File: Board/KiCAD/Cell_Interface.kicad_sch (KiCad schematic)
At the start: 32 parts, among them Q23 2N7002, Q24 2N7002, Q25 2N7002, Q26 2N7002, Q27 IRF9540NSTRLPBF, Q28 IRF9540NSTRLPBF, Q29 IRF9540NSTRLPBF, Q30 IRF9540NSTRLPBF, Q31 IRF9540NSTRLPBF, Q32 2N7002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

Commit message: Add files via upload
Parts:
- removed Q31, Q33: IRF9540NSTRLPBF, IRF9540NSTRLPBF:DPAK254P1524X483-4_3N, symbol IRF9540NSTRLPBF:IRF9540NSTRLPBF
- removed Q32: 2N7002, Package_TO_SOT_SMD:SOT-23, symbol Transistor_FET:2N7002
- removed R70: R_Small, symbol Device:R_Small
- removed R71: R_Small, Resistor_SMD:R_0201_0603Metric, symbol Device:R_Small
- added C49, C50: 100n, Capacitor_SMD:C_0201_0603Metric, symbol Device:C_Small
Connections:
- net 3.3V: now also U6.10 (VS), U6.4 (A1), U7.10 (VS), U7.5 (A0), C49.1, C50.1
- net Cell 2: now also U7.1 (IN+), U7.12 (VBUS), U7.14 (IN-)
- net Cell 3: now also U6.1 (IN+), U6.12 (VBUS), U6.14 (IN-)
- net GND: now also U6.5 (A0), U6.6 (GND), U7.4 (A1), U7.6 (GND), C49.2, C50.2
- net SCL: now also U6.9 (SCL), U7.9 (SCL)
- net SDA: now also U6.8 (SDA), U7.8 (SDA)
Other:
- note added: "Address: 0x40"
- note added: "Address: 0x41"
- note added: "Address: 0x44"
- note added: "Address: 0x45"
- note removed: "Address: 0?"
- note removed: "Address: 3?"
- note removed: "Do you need this switch? What's it for?"
- note removed: "Middle two are left as an exercize to the reader"
- moved on the sheet: C47, C48, Q23, Q24, Q25, Q26, Q27, Q28, Q29, Q30, R17, R18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

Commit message: Add files via upload
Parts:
- removed R18, R19, R61: R_Small, Resistor_SMD:R_0201_0603Metric, symbol Device:R_Small
- added R70, R71, R72: 10k, Resistor_SMD:R_0201_0603Metric, symbol Device:R_Small
- R17: value R_Small -> 10k
- R62, R63, R64, R65, R66, R67, R68, R69: value R_Small -> 10k; footprint (none) -> Resistor_SMD:R_0201_0603Metric
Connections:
- net Cell_Balancer_2: now also R70.1
- net Cell_Balancer_3: now also R71.1
- net Cell_Balancer_4: now also R72.1
- net GND: now also R70.2, R71.2, R72.2

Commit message: Add files via upload
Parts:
- removed Q27, Q28, Q29, Q30: IRF9540NSTRLPBF, IRF9540NSTRLPBF:DPAK254P1524X483-4_3N, symbol IRF9540NSTRLPBF:IRF9540NSTRLPBF
- added Q5, Q6, Q7, Q8: BSS83P, Package_TO_SOT_SMD:SOT-23, symbol Transistor_FET:BSS83P
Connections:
- net Cell 1: now also Q8.3 (D)
- net Cell 2: now also Q7.3 (D)
- net Cell 3: now also Q6.3 (D)
- net Cell 4: now also Q5.3 (D)
- net at Q25.3 (D), R64.2: now also Q6.1 (G)
- net at R68.1: now also Q6.2 (S)
- net at Q23.3 (D), R62.2: now also Q8.1 (G)
- net at R66.1: now also Q8.2 (S)
- net at Q24.3 (D), R63.2: now also Q7.1 (G)
- net at Q26.3 (D), R65.2: now also Q5.1 (G)
- net at R67.1: now also Q7.2 (S)
- net at R69.1: now also Q5.2 (S)
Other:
- moved on the sheet: R62, R64, R65, R66, R67, R68, R69

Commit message: Add files via upload
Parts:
- C47, C48, C49, C50: footprint Capacitor_SMD:C_0201_0603Metric -> Capacitor_SMD:C_0603_1608Metric
- R17, R62, R63, R64, R65, R66, R67, R68, R69, R70, R71, R72, R74: footprint Resistor_SMD:R_0201_0603Metric -> Resistor_SMD:R_0603_1608Metric
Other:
- note removed: "User MUST place batteries starting at Cell 1. Unused cells MUST be bypassed on carrier PCB."
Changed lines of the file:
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@@
 	(text "To battey cells: 1, 2, 3, or 4 cells"
 		(exclude_from_sim no)
-		(at 146.05 110.49 0)
+		(at 139.7 109.22 0)
 		(effects
 			(font
@@
 		)
 	)
-	(text "User MUST place batteries starting at Cell 1.\nUnused cells MUST be bypassed on carrier PCB.\n"
-		(exclude_from_sim no)
-		(at 147.32 114.3 0)
-		(effects
-			(font
-				(size 1.27 1.27)
-			)
-		)
-	)
 	(junction
 		(at 50.8 139.7)
@@
 			)
 		)
-		(property "Footprint" "Resistor_SMD:R_0201_0603Metric"
+		(property "Footprint" "Resistor_SMD:R_0603_1608Metric"
 			(at 72.39 130.81 0)
 			(effects
@@
 			)
 		)
-		(property "Footprint" "Resistor_SMD:R_0201_0603Metric"
+		(property "Footprint" "Resistor_SMD:R_0603_1608Metric"
 			(at 82.55 118.11 0)
 			(effects
@@
 			)
 		)
-		(property "Footprint" "Resistor_SMD:R_0201_0603Metric"
+		(property "Footprint" "Resistor_SMD:R_0603_1608Metric"
 			(at 81.28 49.53 0)
 			(effects
@@
 			)
 		)
-		(property "Footprint" "Resistor_SMD:R_0201_0603Metric"
+		(property "Footprint" "Resistor_SMD:R_0603_1608Metric"
 			(at 97.79 93.98 0)
 			(effects
@@
 			)
 		)
-		(property "Footprint" "Resistor_SMD:R_0201_0603Metric"
+		(property "Footprint" "Resistor_SMD:R_0603_1608Metric"
 			(at 110.49 39.37 0)
 			(effects
@@
 			)
 		)
-		(property "Footprint" "Resistor_SMD:R_0201_0603Metric"
+		(property "Footprint" "Resistor_SMD:R_0603_1608Metric"
 			(at 72.39 168.91 0)
 			(effects
@@
 			)
 		)
-		(property "Footprint" "Resistor_SMD:R_0201_0603Metric"
+		(property "Footprint" "Resistor_SMD:R_0603_1608Metric"
 			(at 97.79 125.73 0)
 			(effects
@@
 			)
 		)
-		(property "Footprint" "Resistor_SMD:R_0201_0603Metric"
+		(property "Footprint" "Resistor_SMD:R_0603_1608Metric"
 			(at 72.39 64.77 0)
 			(effects
@@
 			)
 		)
-		(property "Footprint" "Capacitor_SMD:C_0201_0603Metric"
+		(property "Footprint" "Capacitor_SMD:C_0603_1608Metric"
 			(at 44.45 139.7 0)
 			(effects
@@
 			)
 		)
-		(property "Footprint" "Capacitor_SMD:C_0201_0603Metric"
+		(property "Footprint" "Capacitor_SMD:C_0603_1608Metric"
 			(at 44.45 101.6 0)
 			(effects
@@
 			)
 		)
-		(property "Footprint" "Resistor_SMD:R_0201_0603Metric"
+		(property "Footprint" "Resistor_SMD:R_0603_1608Metric"
 			(at 97.79 163.83 0)
 			(effects
@@
 			)
 		)
-		(property "Footprint" "Resistor_SMD:R_0201_0603Metric"
+		(property "Footprint" "Resistor_SMD:R_0603_1608Metric"
 			(at 72.39 99.06 0)
 			(effects
@@
 			)
 		)
-		(property "Footprint" "Resistor_SMD:R_0201_0603Metric"
+		(property "Footprint" "Resistor_SMD:R_0603_1608Metric"
 			(at 97.79 59.69 0)
 			(effects
@@
 			)
 		)
-		(property "Footprint" "Resistor_SMD:R_0201_0603Metric"
+		(property "Footprint" "Resistor_SMD:R_0603_1608Metric"
 			(at 80.01 85.09 0)
 			(effects
@@
 			)
 		)
-		(property "Footprint" "Resistor_SMD:R_0201_0603Metric"
+		(property "Footprint" "Resistor_SMD:R_0603_1608Metric"
 			(at 82.55 152.4 0)
 			(effects
@@
 			)
 		)
-		(property "Footprint" "Capacitor_SMD:C_0201_0603Metric"
+		(property "Footprint" "Capacitor_SMD:C_0603_1608Metric"
 			(at 54.61 25.4 0)
 			(effects
@@
 			)
 		)
-		(property "Footprint" "Capacitor_SMD:C_0201_0603Metric"
+		(property "Footprint" "Capacitor_SMD:C_0603_1608Metric"
 			(at 45.72 63.5 0)
 			(effects

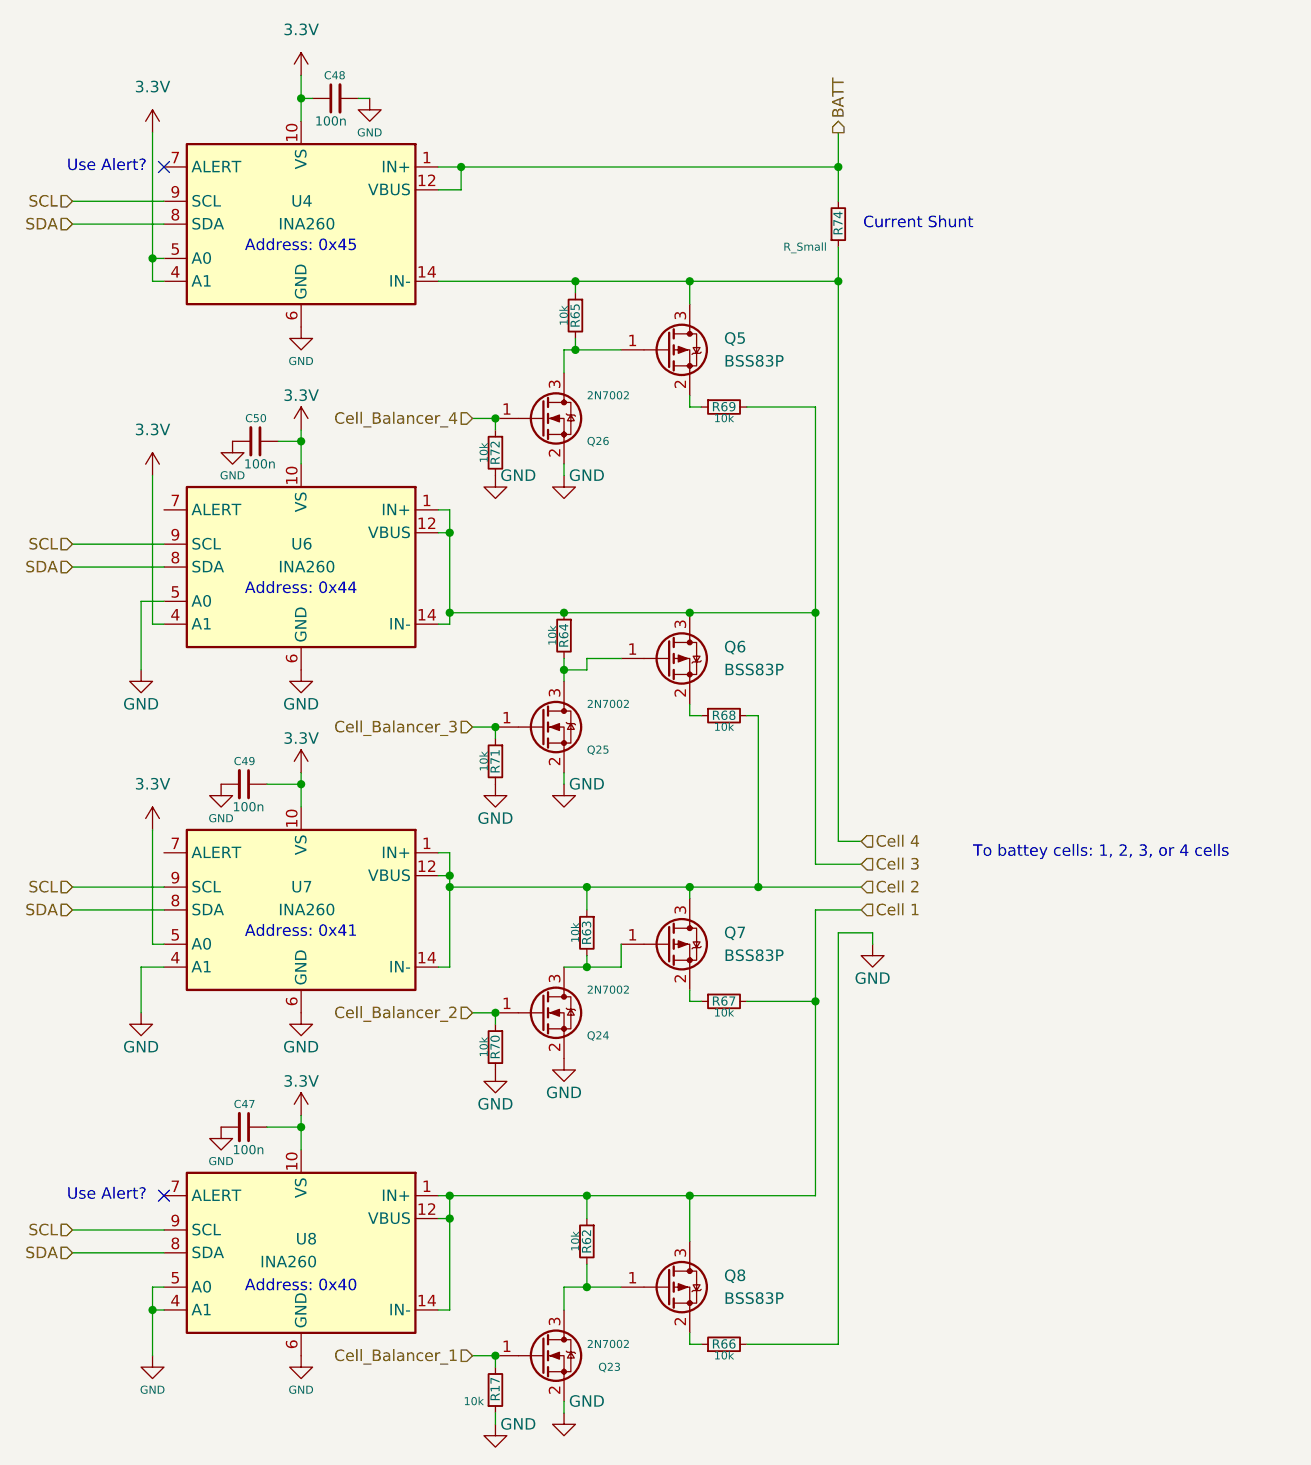
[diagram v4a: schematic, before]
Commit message: Schematic: - Fixed FDI plug - Added thermistor connectors - Added a bunch of NCs using KiCAD NC tool - Added filter cap back into battery current shunt - Added bypass cap to LTC - Removed Cell 4 INA260 because the LTC does current, voltage of that top cell! Board Layout: - Chewed out team for not reading the BQ's datasheet, specifically Section 11 - Relayed out power stream using Section 11 as a refernce - Changed some footprints, mostly reducing size to 0603 - Positioned things optimally given what I thought made sense (dangerous, I know) - Fixed ground planes Other: - Removed PRL and CACHE files from the repo.
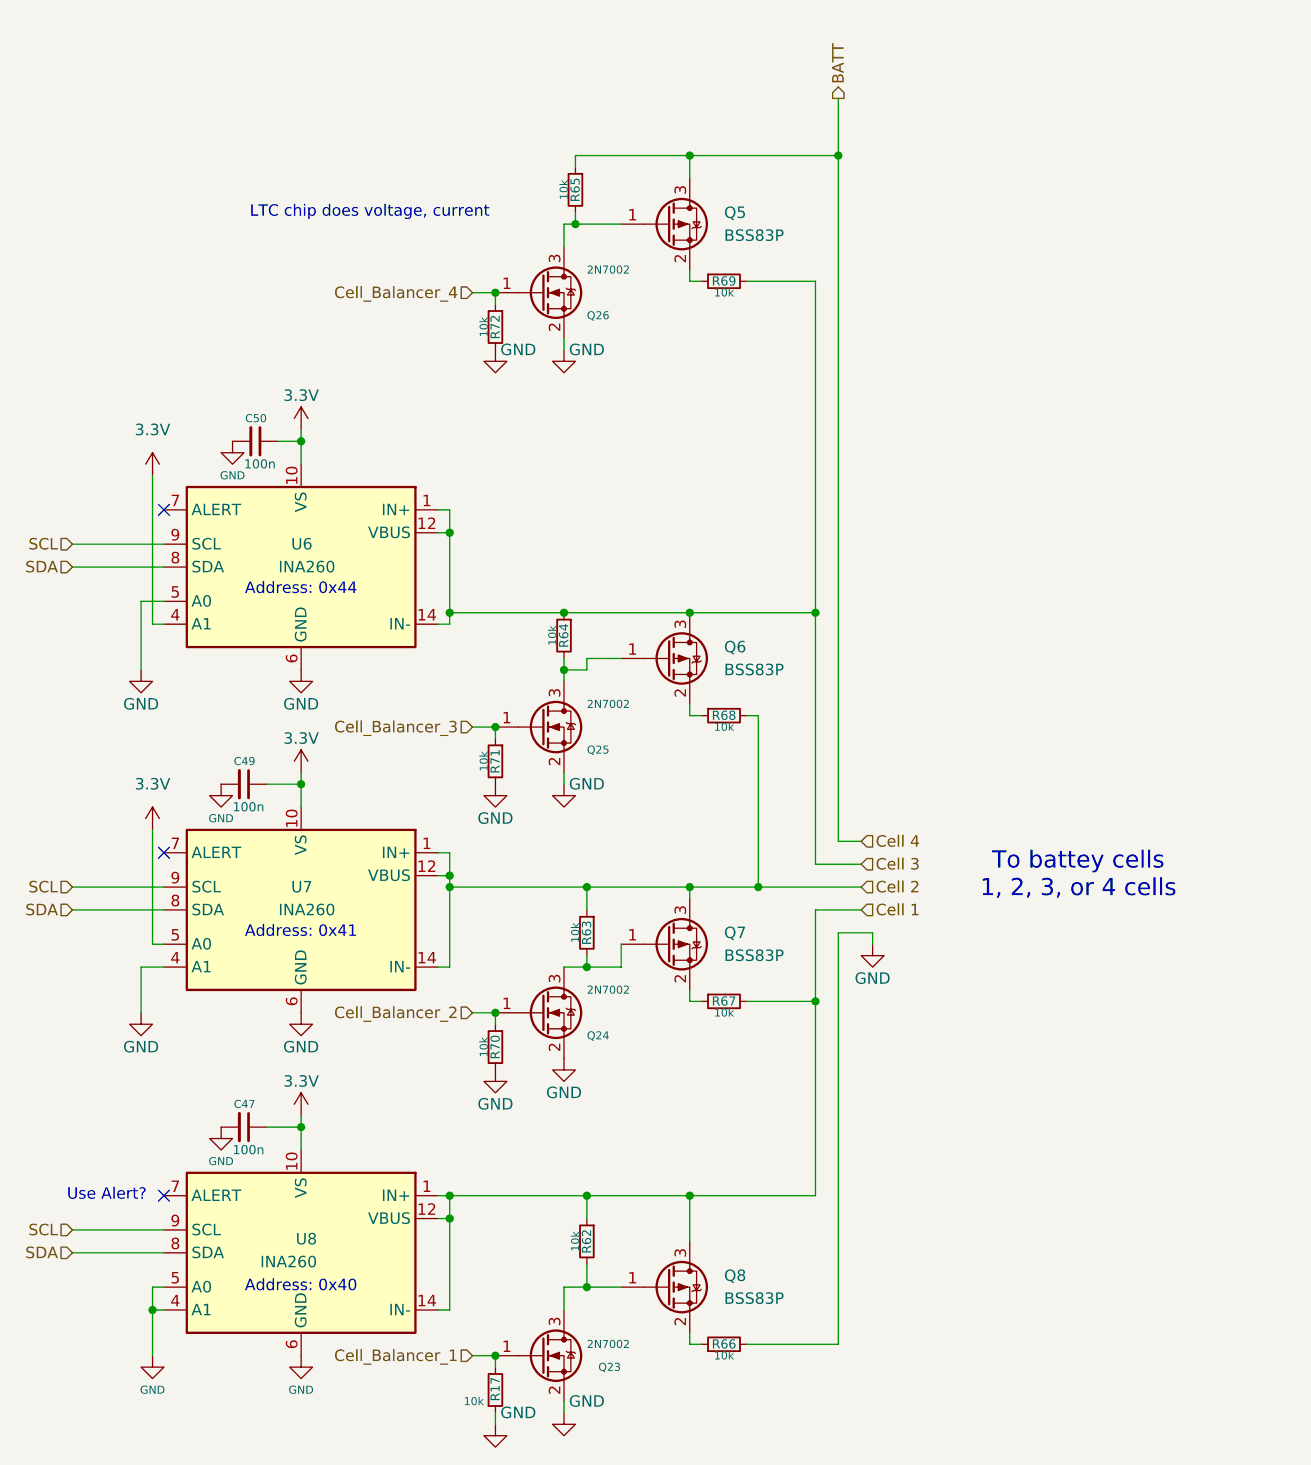
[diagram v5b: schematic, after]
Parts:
- removed C48: 100n, Capacitor_SMD:C_0603_1608Metric, symbol Device:C_Small
- removed R74: R_Small, Resistor_SMD:R_0603_1608Metric, symbol Device:R_Small
- removed U4: INA260, Package_SO:TSSOP-16_4.4x5mm_P0.65mm, symbol Sensor:INA260
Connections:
- net Cell 4 is gone; now on net BATT: Q5.3 (D), R65.1
- no-connect marks 2 -> 3
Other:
- note added: "LTC chip does voltage, current"
- note added: "To battey cells 1, 2, 3, or 4 cells"
- note removed: "Address: 0x45"
- note removed: "Current Shunt"
- note removed: "To battey cells: 1, 2, 3, or 4 cells"
- moved on the sheet: Q26, Q5, R65, R69, R72

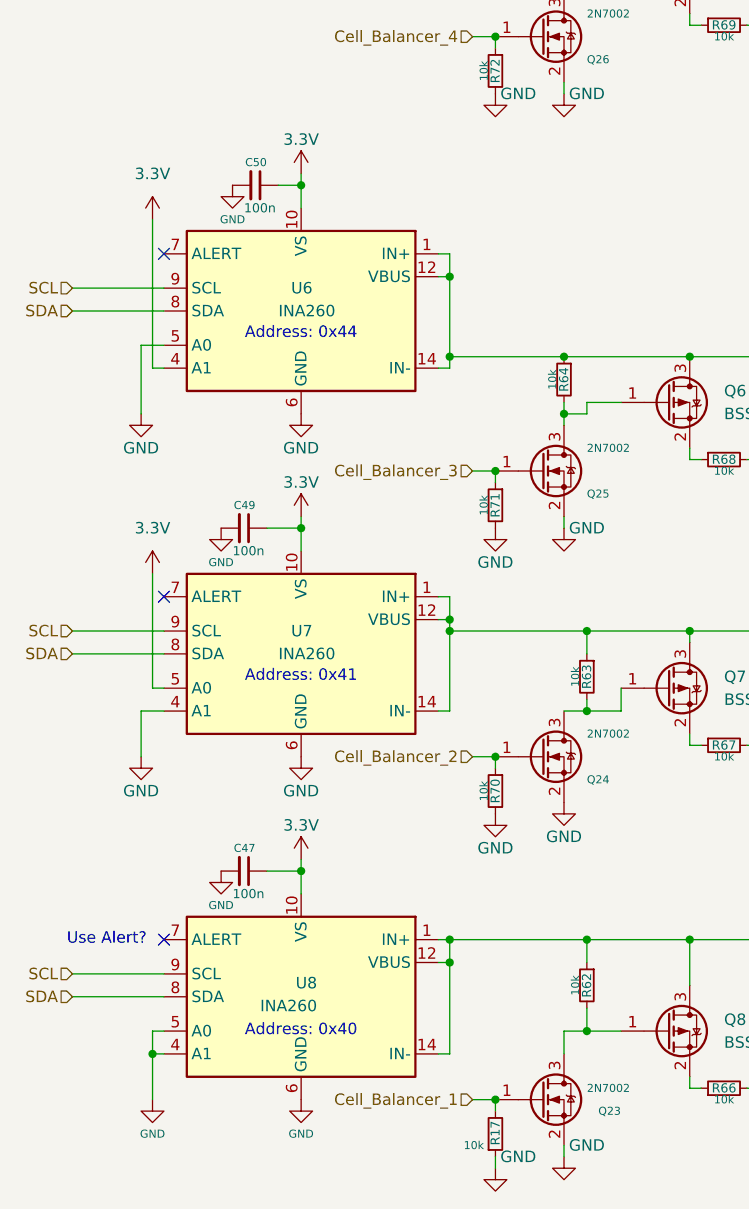
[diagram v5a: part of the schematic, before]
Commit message: Completed PCB Traceout
PCB Layout and traceout completed

@KeytarGoblin @Danish2PSU  @andrewgreenberg
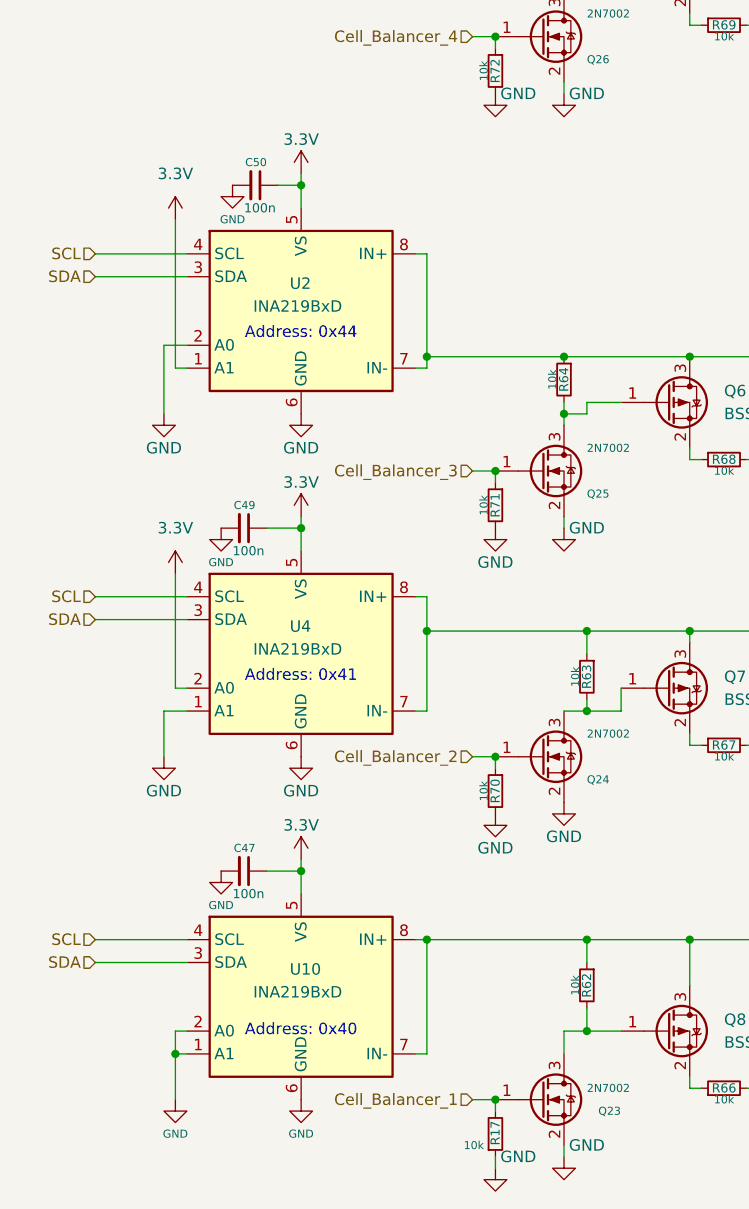
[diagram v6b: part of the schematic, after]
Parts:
- removed U6, U7, U8: INA260, Package_SO:TSSOP-16_4.4x5mm_P0.65mm, symbol Sensor:INA260
- added U10, U2, U4: INA219BxD, Package_SO:SOIC-8_3.9x4.9mm_P1.27mm, symbol Sensor_Energy:INA219BxD
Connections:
- net 3.3V: now also U10.5 (VS), U2.1 (A1), U2.5 (VS), U4.2 (A0), U4.5 (VS)
- net Cell 1: now also U10.7 (IN-), U10.8 (IN+)
- net Cell 2: now also U4.7 (IN-), U4.8 (IN+)
- net Cell 3: now also U2.7 (IN-), U2.8 (IN+)
- net GND: now also U10.1 (A1), U10.2 (A0), U10.6 (GND), U2.2 (A0), U2.6 (GND), U4.1 (A1), U4.6 (GND)
- net SCL: now also U10.4 (SCL), U2.4 (SCL), U4.4 (SCL)
- net SDA: now also U10.3 (SDA), U2.3 (SDA), U4.3 (SDA)
- no-connect marks 3 -> 0
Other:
- note removed: "Use Alert?"

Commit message: current form
current form of pcb @andrewgreenberg
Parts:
- removed U10, U2, U4: INA219BxD, Package_SO:SOIC-8_3.9x4.9mm_P1.27mm, symbol Sensor_Energy:INA219BxD
- added U6, U7, U8: INA219AxDCN, Package_TO_SOT_SMD:SOT-23-8, symbol Sensor_Energy:INA219AxDCN
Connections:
- net 3.3V: now also U6.1 (A1), U6.5 (VS), U7.2 (A0), U7.5 (VS), U8.5 (VS)
- net Cell 1: now also U8.7 (IN-), U8.8 (IN+)
- net Cell 2: now also U7.7 (IN-), U7.8 (IN+)
- net Cell 3: now also U6.7 (IN-), U6.8 (IN+)
- net GND: now also U6.2 (A0), U6.6 (GND), U7.1 (A1), U7.6 (GND), U8.1 (A1), U8.2 (A0), U8.6 (GND)
- net SCL: now also U6.4 (SCL), U7.4 (SCL), U8.4 (SCL)
- net SDA: now also U6.3 (SDA), U7.3 (SDA), U8.3 (SDA)
